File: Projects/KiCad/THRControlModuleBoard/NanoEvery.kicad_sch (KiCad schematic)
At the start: 46 parts, among them IC1 LTC1480CN8#PBF, IC2 LTC1480CN8#PBF, J5 Conn_01x04_Socket, J6 Conn_01x04_Socket, U2 MCP2562-E-P, U3 MCP2515-I/P, U4 TLP222A, U5 MAX31855, Y1 8MHz

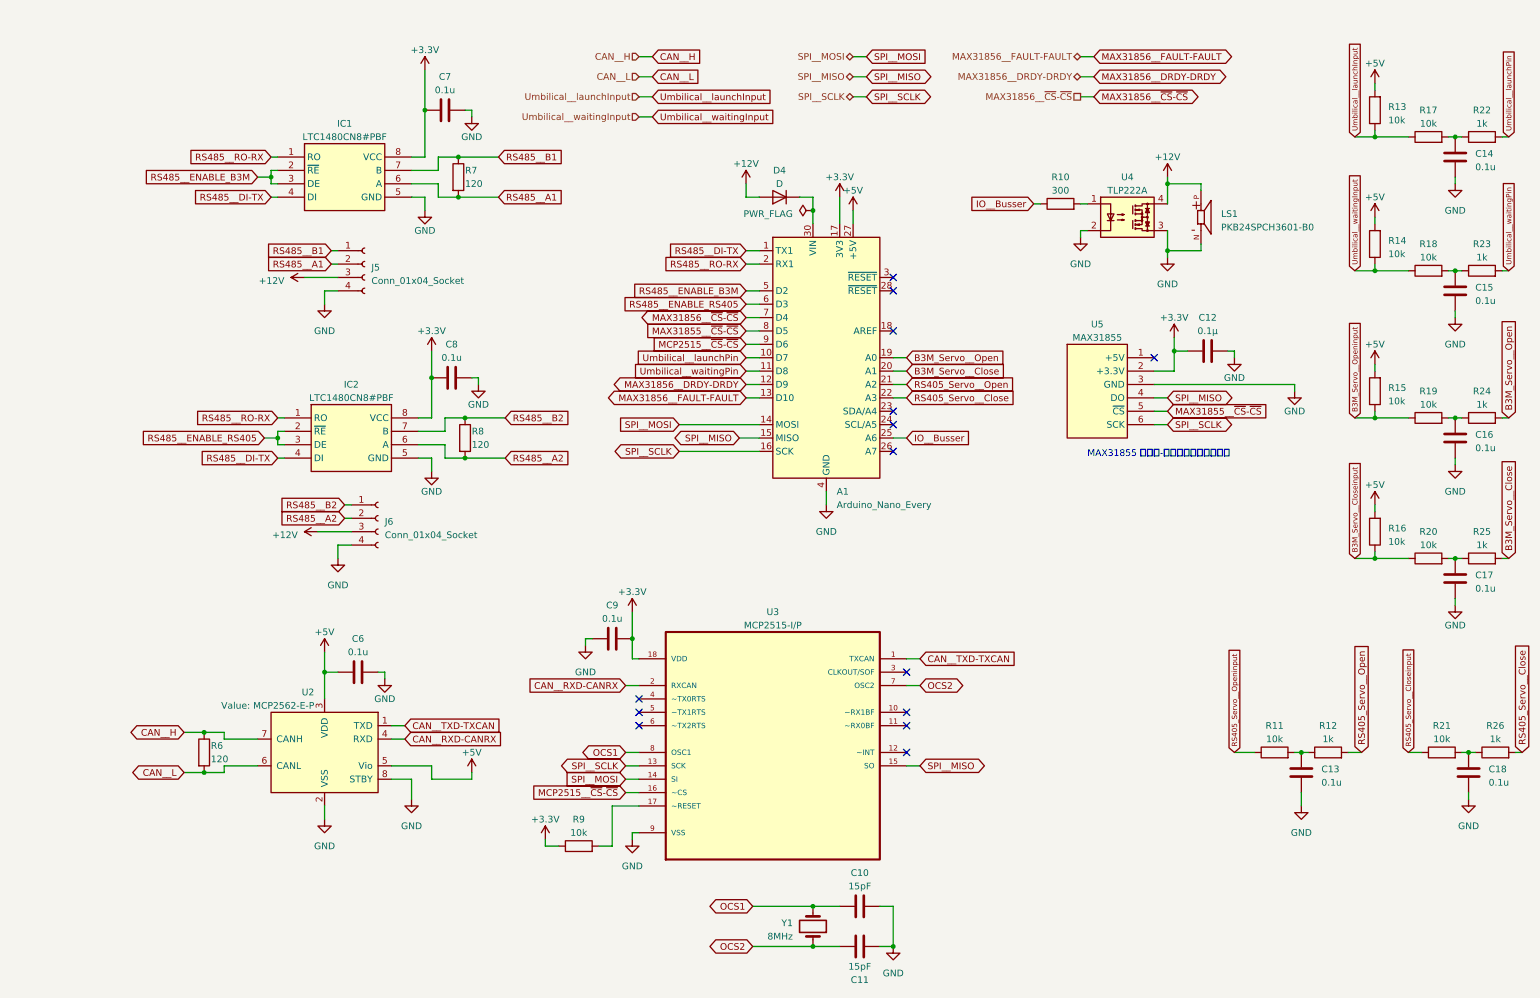
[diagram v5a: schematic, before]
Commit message: 基板形状を決定。部品を配置中
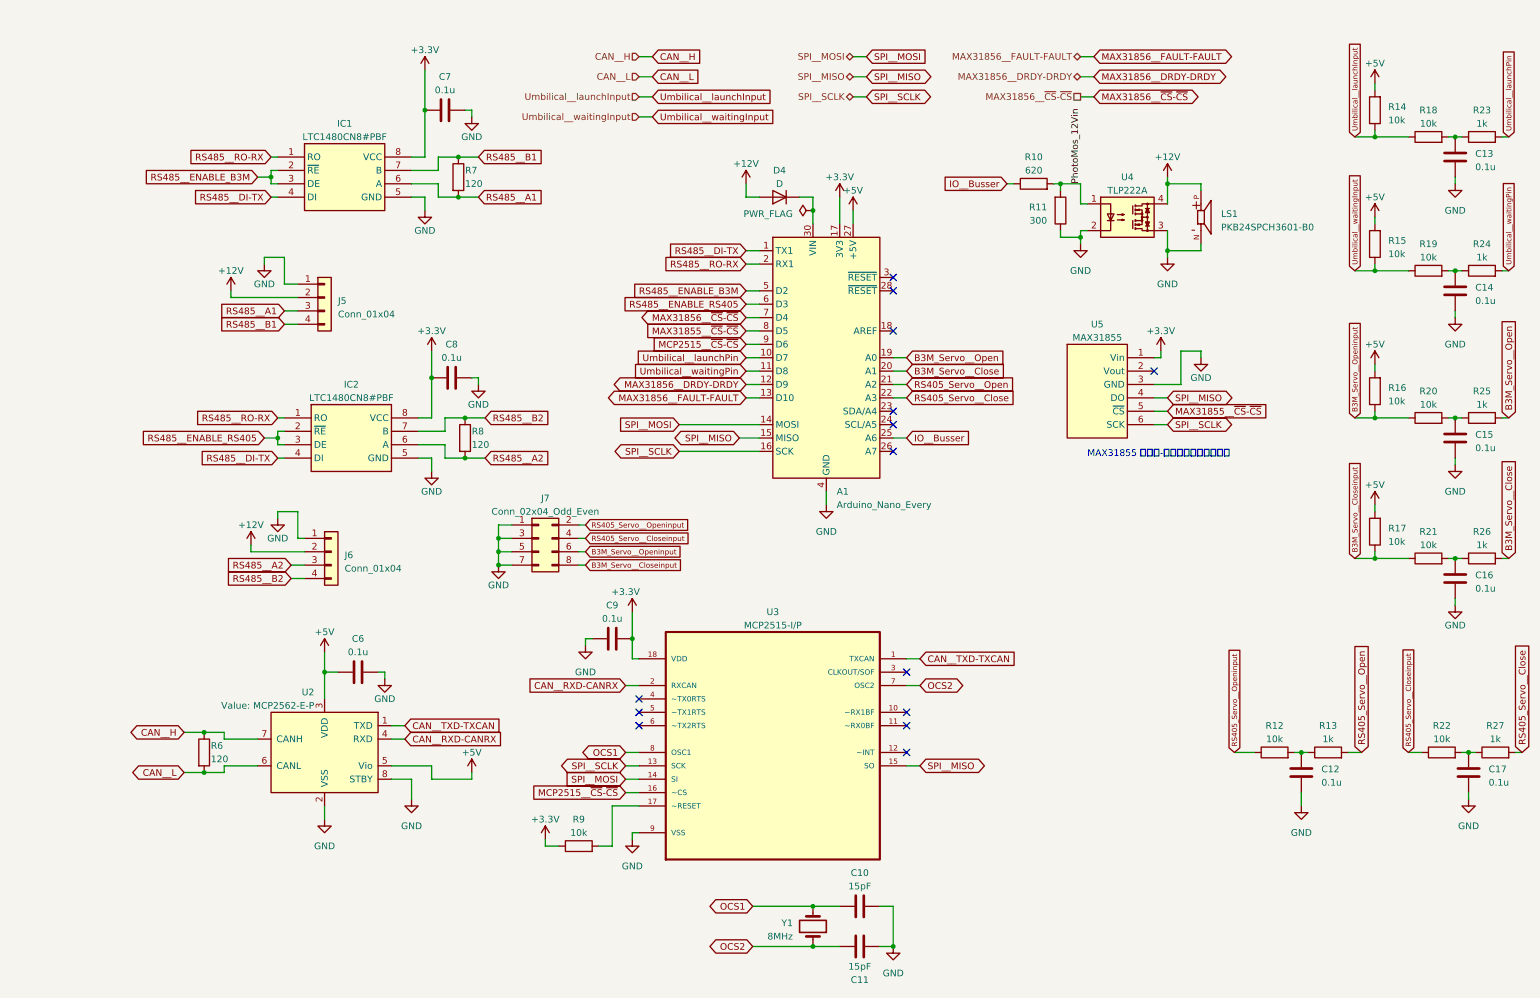
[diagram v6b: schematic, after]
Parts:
- removed C12: 0.1μ, Capacitor_SMD:C_0603_1608Metric_Pad1.08x0.95mm_HandSolder, symbol Device:C
- removed J5, J6: Conn_01x04_Socket, CONNECTOR:CONNECTOR_4-STRAIGHT, symbol Connector:Conn_01x04_Socket
- added J5, J6: Conn_01x04, CONNECTOR:CONNECTOR_4-STRAIGHT, symbol Connector_Generic:Conn_01x04
- added J7: Conn_02x04_Odd_Even, Hirose_Connector:Hirose_DF11B-8DP-2DS, symbol Connector_Generic:Conn_02x04_Odd_Even
- added R11: 300, symbol Device:R
- R10: value 300 -> 620
- renumbered C13 to C12, C14 to C13, C15 to C14, C16 to C15, C17 to C16, C18 to C17, R11 to R12, R12 to R13, R13 to R14, R14 to R15, R15 to R16, R16 to R17, R17 to R18, R18 to R19, R19 to R20, R20 to R21, R21 to R22, R22 to R23, R23 to R24, R24 to R25, R25 to R26, R26 to R27
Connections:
- net +12V: now also J5.2 (Pin_2), J6.2 (Pin_2)
- net +3.3V: now also U5.1 (Vin); no longer U5.2 (+3.3V)
- net B3M_Servo__Closeinput: now also J7.8 (Pin_8)
- net B3M_Servo__Openinput: now also J7.6 (Pin_6)
- net GND: now also J5.1 (Pin_1), J6.1 (Pin_1), J7.1 (Pin_1), J7.3 (Pin_3), J7.5 (Pin_5), J7.7 (Pin_7), R11.1
- net RS405_Servo__Closeinput: now also J7.4 (Pin_4)
- net RS405_Servo__Openinput: now also J7.2 (Pin_2)
- net RS485__A1: now also J5.3 (Pin_3)
- net RS485__A2: now also J6.3 (Pin_3)
- net RS485__B1: now also J5.4 (Pin_4)
- net RS485__B2: now also J6.4 (Pin_4)
- net PhotoMos_12Vin: now reaches R10.2, U4.1
- net PhotoMos_12Vin: now also R11.2
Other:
- moved on the sheet: R10

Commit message: 攻めた設計になってるけど動いてくれ…
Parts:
- removed D4: D, Diode_SMD:D_SOD-123, symbol Device:D
- removed R14, R15, R16, R17: 10k, Resistor_SMD:R_0603_1608Metric_Pad0.98x0.95mm_HandSolder, symbol Device:R
- added D4, D5: MM3Zxx, Diode_SMD:D_SOD-323F, symbol Diode:MM3Zxx
- R11: footprint (none) -> Resistor_SMD:R_0603_1608Metric_Pad0.98x0.95mm_HandSolder
- renumbered J5 to J4, J6 to J5, J7 to J6, R18 to R14, R19 to R15, R20 to R16, R21 to R17, R22 to R18, R23 to R19, R24 to R20, R25 to R21, R26 to R22, R27 to R23
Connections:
- net +12V: now also A1.30 (VIN), D4.1 (K), D5.1 (K)
- net GND: now also D4.2 (A), D5.2 (A)

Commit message: ボード図を更新
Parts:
- C12, C13, C14, C15, C16, C17: value 0.1u -> 0.1uF; footprint Capacitor_SMD:C_0805_2012Metric_Pad1.18x1.45mm_HandSolder -> Capacitor_SMD:C_0603_1608Metric_Pad1.08x0.95mm_HandSolder
- C6, C7, C8, C9: value 0.1u -> 0.1uF
- U2: value MCP2562-E-P -> Value: Value: Value: Value: MCP2562-E-P
- Y1: footprint Crystal:Crystal_HC49-U_Vertical -> Crystal:Crystal_HC49-4H_Vertical
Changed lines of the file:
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@@
       (effects (font (size 1.27 1.27)) (justify left))
     )
-    (property "Value" "0.1u" (at 269.24 118.745 0)
-      (effects (font (size 1.27 1.27)) (justify left))
-    )
-    (property "Footprint" "Capacitor_SMD:C_0805_2012Metric_Pad1.18x1.45mm_HandSolder" (at 266.3952 120.65 0)
+    (property "Value" "0.1uF" (at 269.24 118.745 0)
+      (effects (font (size 1.27 1.27)) (justify left))
+    )
+    (property "Footprint" "Capacitor_SMD:C_0603_1608Metric_Pad1.08x0.95mm_HandSolder" (at 266.3952 120.65 0)
       (effects (font (size 1.27 1.27)) hide)
     )
@@
       (effects (font (size 1.27 1.27)) (justify left))
     )
-    (property "Value" "0.1u" (at 269.24 92.075 0)
-      (effects (font (size 1.27 1.27)) (justify left))
-    )
-    (property "Footprint" "Capacitor_SMD:C_0805_2012Metric_Pad1.18x1.45mm_HandSolder" (at 266.3952 93.98 0)
+    (property "Value" "0.1uF" (at 269.24 92.075 0)
+      (effects (font (size 1.27 1.27)) (justify left))
+    )
+    (property "Footprint" "Capacitor_SMD:C_0603_1608Metric_Pad1.08x0.95mm_HandSolder" (at 266.3952 93.98 0)
       (effects (font (size 1.27 1.27)) hide)
     )
@@
       (effects (font (size 1.27 1.27)))
     )
-    (property "Value" "0.1u" (at 74.93 74.93 90)
+    (property "Value" "0.1uF" (at 74.93 74.93 90)
       (effects (font (size 1.27 1.27)))
     )
@@
       (effects (font (size 1.27 1.27)) (justify left))
     )
-    (property "Value" "0.1u" (at 269.24 64.135 0)
-      (effects (font (size 1.27 1.27)) (justify left))
-    )
-    (property "Footprint" "Capacitor_SMD:C_0805_2012Metric_Pad1.18x1.45mm_HandSolder" (at 266.3952 66.04 0)
+    (property "Value" "0.1uF" (at 269.24 64.135 0)
+      (effects (font (size 1.27 1.27)) (justify left))
+    )
+    (property "Footprint" "Capacitor_SMD:C_0603_1608Metric_Pad1.08x0.95mm_HandSolder" (at 266.3952 66.04 0)
       (effects (font (size 1.27 1.27)) hide)
     )
@@
       (effects (font (size 1.27 1.27)))
     )
-    (property "Value" "0.1u" (at 57.15 130.81 90)
+    (property "Value" "0.1uF" (at 57.15 130.81 90)
       (effects (font (size 1.27 1.27)))
     )
@@
       (effects (font (size 1.27 1.27)))
     )
-    (property "Value" "0.1u" (at 73.66 24.13 90)
+    (property "Value" "0.1uF" (at 73.66 24.13 90)
       (effects (font (size 1.27 1.27)))
     )
@@
       (effects (font (size 1.27 1.27)) (justify right))
     )
-    (property "Footprint" "Crystal:Crystal_HC49-U_Vertical" (at 143.51 182.88 0)
+    (property "Footprint" "Crystal:Crystal_HC49-4H_Vertical" (at 143.51 182.88 0)
       (effects (font (size 1.27 1.27)) hide)
     )
@@
       (effects (font (size 1.27 1.27)) (justify left))
     )
-    (property "Value" "0.1u" (at 271.78 155.575 0)
-      (effects (font (size 1.27 1.27)) (justify left))
-    )
-    (property "Footprint" "Capacitor_SMD:C_0805_2012Metric_Pad1.18x1.45mm_HandSolder" (at 268.9352 157.48 0)
+    (property "Value" "0.1uF" (at 271.78 155.575 0)
+      (effects (font (size 1.27 1.27)) (justify left))
+    )
+    (property "Footprint" "Capacitor_SMD:C_0603_1608Metric_Pad1.08x0.95mm_HandSolder" (at 268.9352 157.48 0)
       (effects (font (size 1.27 1.27)) hide)
     )
@@
       (effects (font (size 1.27 1.27)))
     )
-    (property "Value" "0.1u" (at 105.41 124.46 90)
+    (property "Value" "0.1uF" (at 105.41 124.46 90)
       (effects (font (size 1.27 1.27)))
     )
@@
       (effects (font (size 1.27 1.27)) (justify left))
     )
-    (property "Value" "MCP2562-E-P" (at 48.8441 140.97 0) (show_name)
+    (property "Value" "Value: Value: Value: Value: MCP2562-E-P" (at 48.8441 140.97 0) (show_name)
       (effects (font (size 1.27 1.27)) (justify left))
     )
@@
       (effects (font (size 1.27 1.27)) (justify left))
     )
-    (property "Value" "0.1u" (at 269.24 38.735 0)
-      (effects (font (size 1.27 1.27)) (justify left))
-    )
-    (property "Footprint" "Capacitor_SMD:C_0805_2012Metric_Pad1.18x1.45mm_HandSolder" (at 266.3952 40.64 0)
+    (property "Value" "0.1uF" (at 269.24 38.735 0)
+      (effects (font (size 1.27 1.27)) (justify left))
+    )
+    (property "Footprint" "Capacitor_SMD:C_0603_1608Metric_Pad1.08x0.95mm_HandSolder" (at 266.3952 40.64 0)
       (effects (font (size 1.27 1.27)) hide)
     )
@@
       (effects (font (size 1.27 1.27)) (justify left))
     )
-    (property "Value" "0.1u" (at 240.03 155.575 0)
-      (effects (font (size 1.27 1.27)) (justify left))
-    )
-    (property "Footprint" "Capacitor_SMD:C_0805_2012Metric_Pad1.18x1.45mm_HandSolder" (at 237.1852 157.48 0)
-      (effects (font (size 1.27 1.27)) hide)
-    )
+    (property "Value" "0.1uF" (at 240.03 155.575 0)
+      (effects (font (size 1.27 1.27)) (justify left))
+    )
+    (property "Footprint" "Capacitor_SMD:C_0603_1608Metric_Pad1.08x0.95mm_HandSolder" (at 237.1852 157.48 0)
+      (effects (font (size 1.27 1.27)) hide)
+    )
